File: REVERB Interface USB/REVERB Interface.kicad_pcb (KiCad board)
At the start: 2 copper layers, 90.2 x 95.9 mm, 60 parts, among them J1 RPiZeroW, J2 Iridium, J3 APRS, J4 Antenna, J6 USB_B_Micro, J7 USB, J8 USBPOGO, M1 MountingHole_Pad, M2 MountingHole_Pad, M3 MountingHole_Pad, M4 MountingHole_Pad, M5 PiMount, M6 PiMount, M7 PiMount, M8 PiMount, U1 LSM9DS1BOB, U2 MAX3232, U3 CY7C65213-28PVXI, U4 TXB0104D

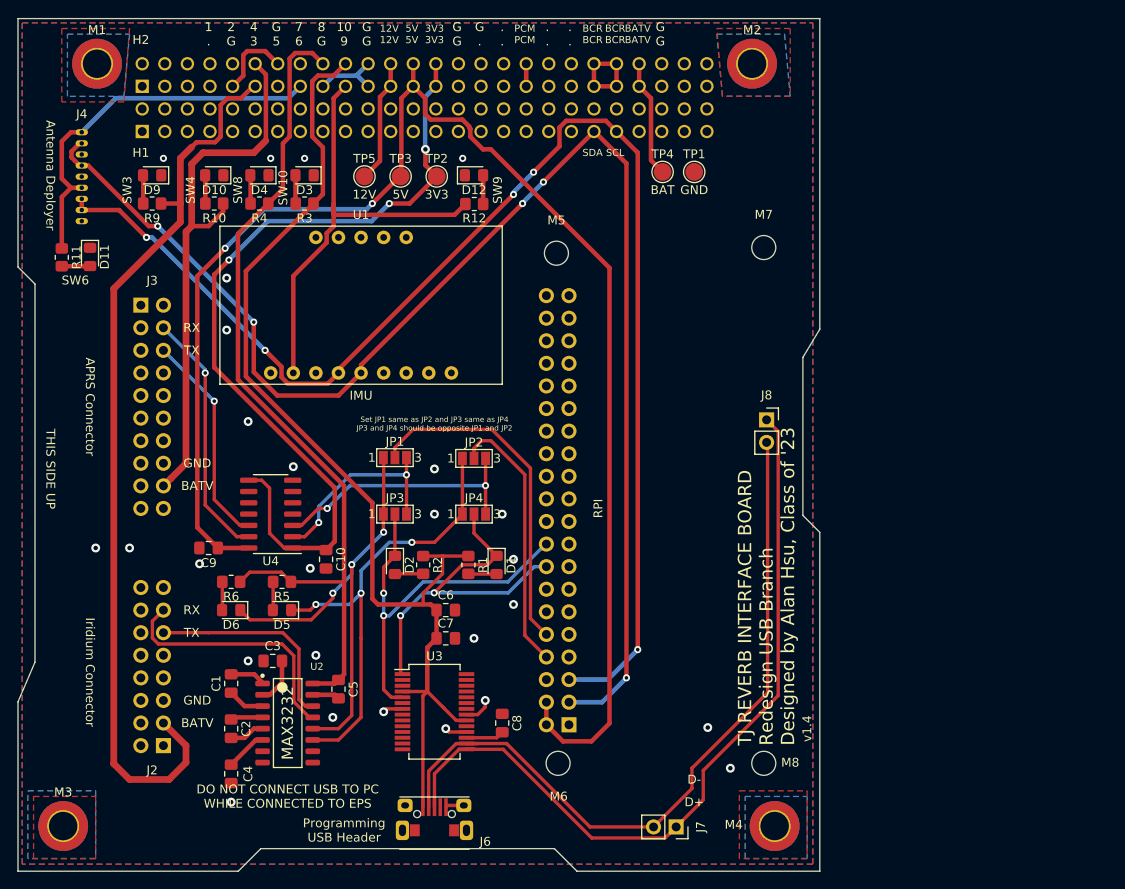
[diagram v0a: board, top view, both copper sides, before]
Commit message: Add decoupling
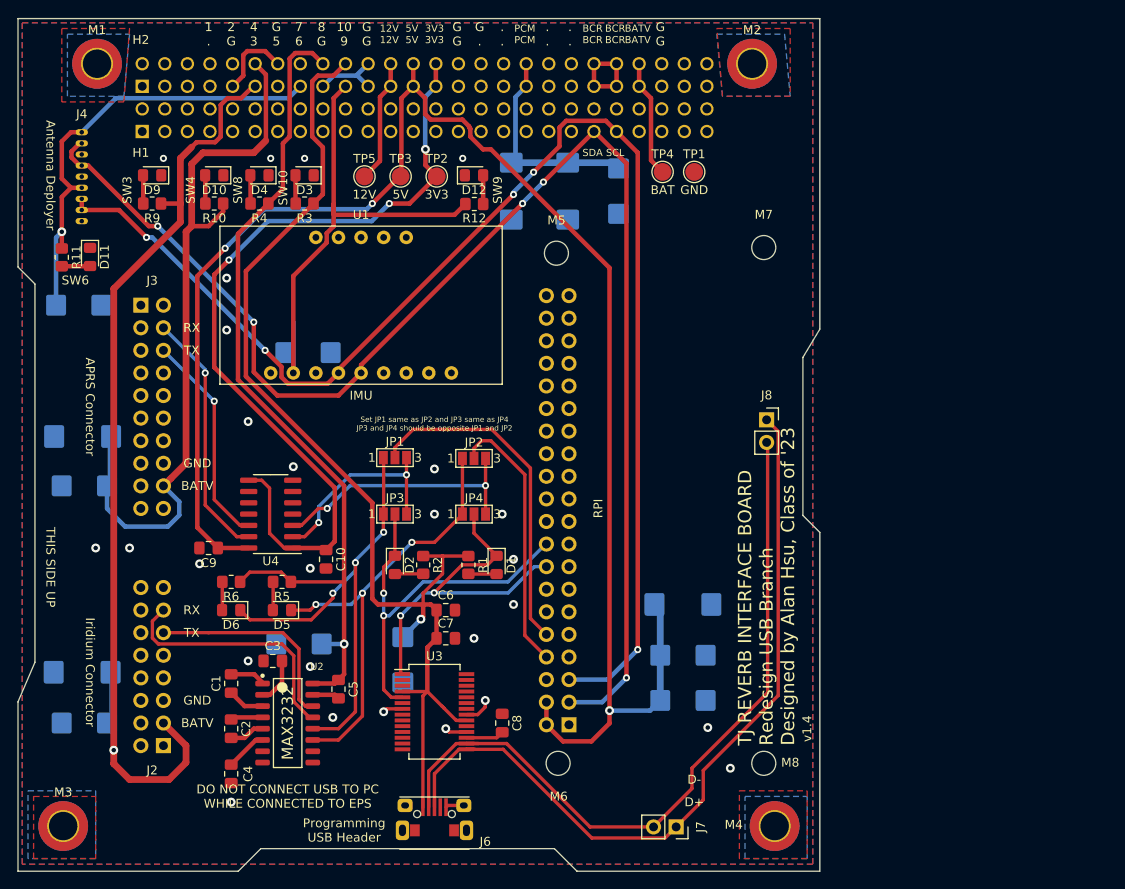
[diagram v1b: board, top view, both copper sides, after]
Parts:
- added C11: 100uF, Capacitor_Tantalum_SMD:CP_EIA-7343-43_Kemet-X_Pad2.25x2.55mm_HandSolder, B.Cu at (181.6, 118.7)
- added C12: 47uF, Capacitor_Tantalum_SMD:CP_EIA-6032-28_Kemet-C_Pad2.25x2.35mm_HandSolder, B.Cu at (181.6, 124.5)
- added C13: 22uF, Capacitor_Tantalum_SMD:CP_EIA-6032-28_Kemet-C_Pad2.25x2.35mm_HandSolder, B.Cu at (181.6, 129.5)
- added C14: 100uF, Capacitor_Tantalum_SMD:CP_EIA-7343-43_Kemet-X_Pad2.25x2.55mm_HandSolder, B.Cu at (114.0, 126.4)
- added C15: 47uF, Capacitor_Tantalum_SMD:CP_EIA-6032-28_Kemet-C_Pad2.25x2.35mm_HandSolder, B.Cu at (114.3, 132.1)
- added C16: 47uF, Capacitor_Tantalum_SMD:CP_EIA-6032-28_Kemet-C_Pad2.25x2.35mm_HandSolder, B.Cu at (113.7, 85.1)
- added C18: 47uF, Capacitor_Tantalum_SMD:CP_EIA-6032-28_Kemet-C_Pad2.25x2.35mm_HandSolder, B.Cu at (139.4, 90.4)
- added C20: 100uF, Capacitor_Tantalum_SMD:CP_EIA-7343-43_Kemet-X_Pad2.25x2.55mm_HandSolder, B.Cu at (162.3, 72.3)
- added C21: 100uF, Capacitor_Tantalum_SMD:CP_EIA-7343-43_Kemet-X_Pad2.25x2.55mm_HandSolder, B.Cu at (168.7, 72.3)
- added C22: 47uF, Capacitor_Tantalum_SMD:CP_EIA-6032-28_Kemet-C_Pad2.25x2.35mm_HandSolder, B.Cu at (174.4, 72.3)
- added C23: 100uF, Capacitor_Tantalum_SMD:CP_EIA-7343-43_Kemet-X_Pad2.25x2.55mm_HandSolder, B.Cu at (114.1, 99.9)
- added C24: 47uF, Capacitor_Tantalum_SMD:CP_EIA-6032-28_Kemet-C_Pad2.25x2.35mm_HandSolder, B.Cu at (114.3, 105.4)
- added C25: 47uF, Capacitor_Tantalum_SMD:CP_EIA-6032-28_Kemet-C_Pad2.25x2.35mm_HandSolder, B.Cu at (138.4, 123.2)
- added C27: 47uF, Capacitor_Tantalum_SMD:CP_EIA-6032-28_Kemet-C_Pad2.25x2.35mm_HandSolder, B.Cu at (150.1, 125.0)
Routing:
- net /SW4: track 61.2 -> 83.0 mm
- net /PCM_IN: track 2.54 -> 24.2 mm
- net +5V: track 170.4 -> 187.6 mm, vias 2 -> 3
- net /SW3: track 104.9 -> 114.2 mm, vias 0 -> 1
- net /SW6: track 43.5 -> 51.7 mm, vias 0 -> 1
- net /SW9: track 51.1 -> 56.8 mm
- net /SW10: track 125.2 -> 129.8 mm, vias 0 -> 1
- net /SW8: track 97.7 -> 100.3 mm, vias 0 -> 1
- net /T1IN: track 52.0 -> 50.7 mm

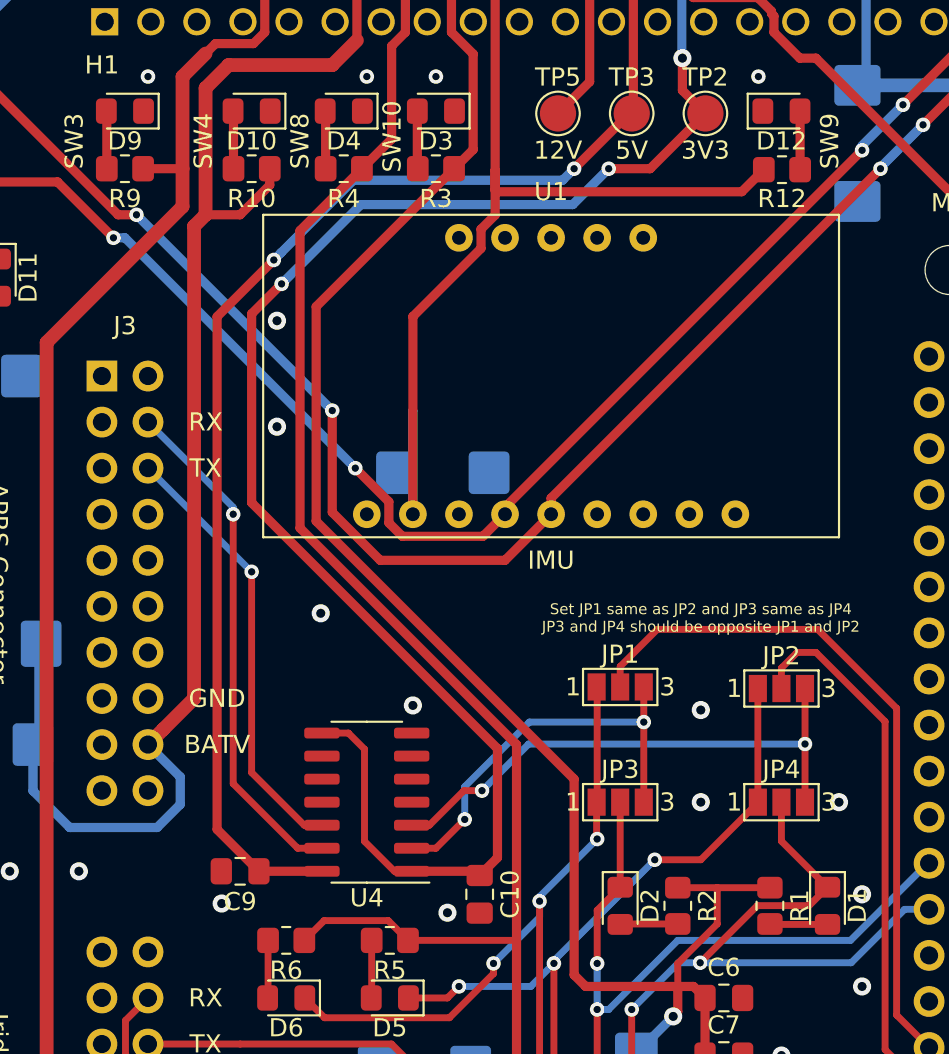
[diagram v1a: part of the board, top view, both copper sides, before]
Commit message: fix imu implementation, add bno055 compatibility
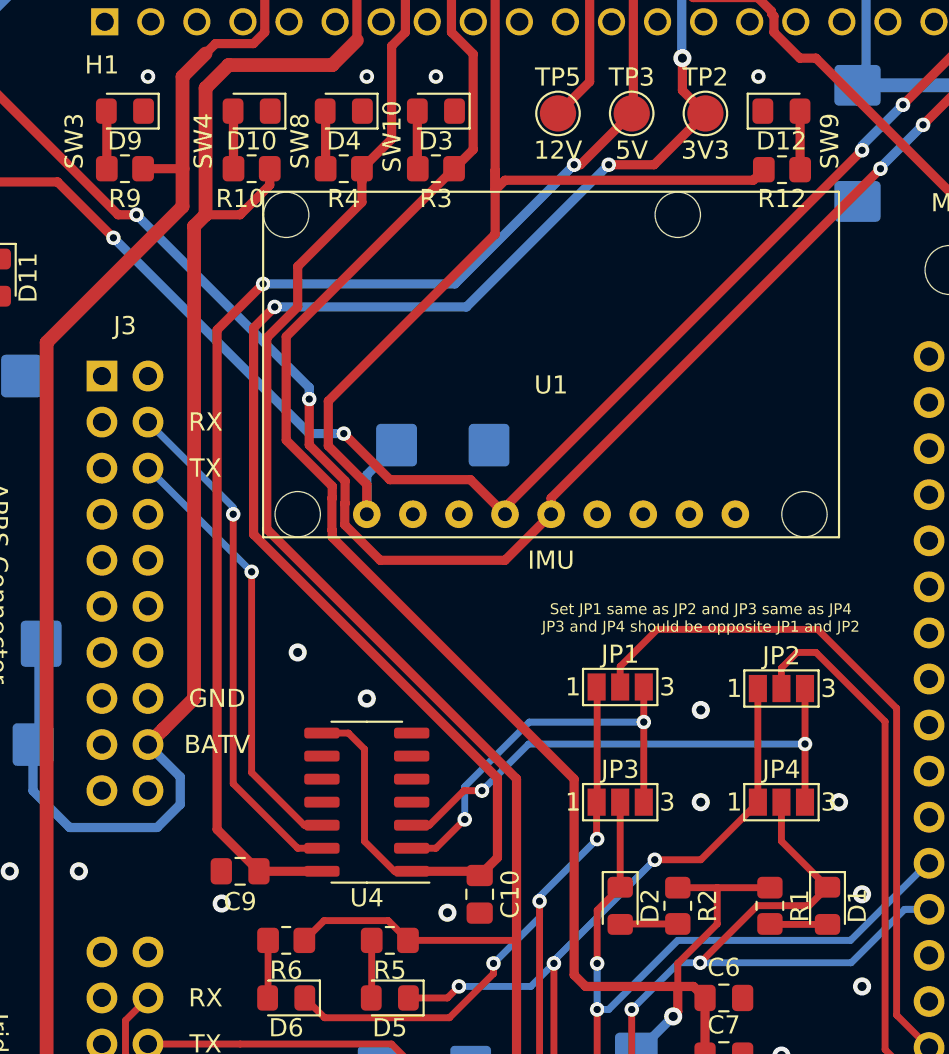
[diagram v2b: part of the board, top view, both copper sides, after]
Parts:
- U1: value LSM9DS1BOB -> IMU; footprint REVERB Interface:LSM9DS1BOB -> REVERB Interface:LSM9DS1-BNO055
- moved C18 1.52 mm to (139.4, 88.9)
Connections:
- U1 pad 1: (no net) -> /SW9
- U1 pad 3: (no net) -> GND
- U1 pad 4: (no net) -> /EPSSCL
- U1 pad 5: (no net) -> /EPSSDA
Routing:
- net /EPSSCL: track 152.9 -> 151.2 mm
- net /SW8: track 100.3 -> 101.8 mm
- net /SW9: track 56.8 -> 58.3 mm
- net /SW10: track 129.8 -> 131.2 mm
- net +3V3: track 95.2 -> 94.6 mm
- net GND: vias 27 -> 25

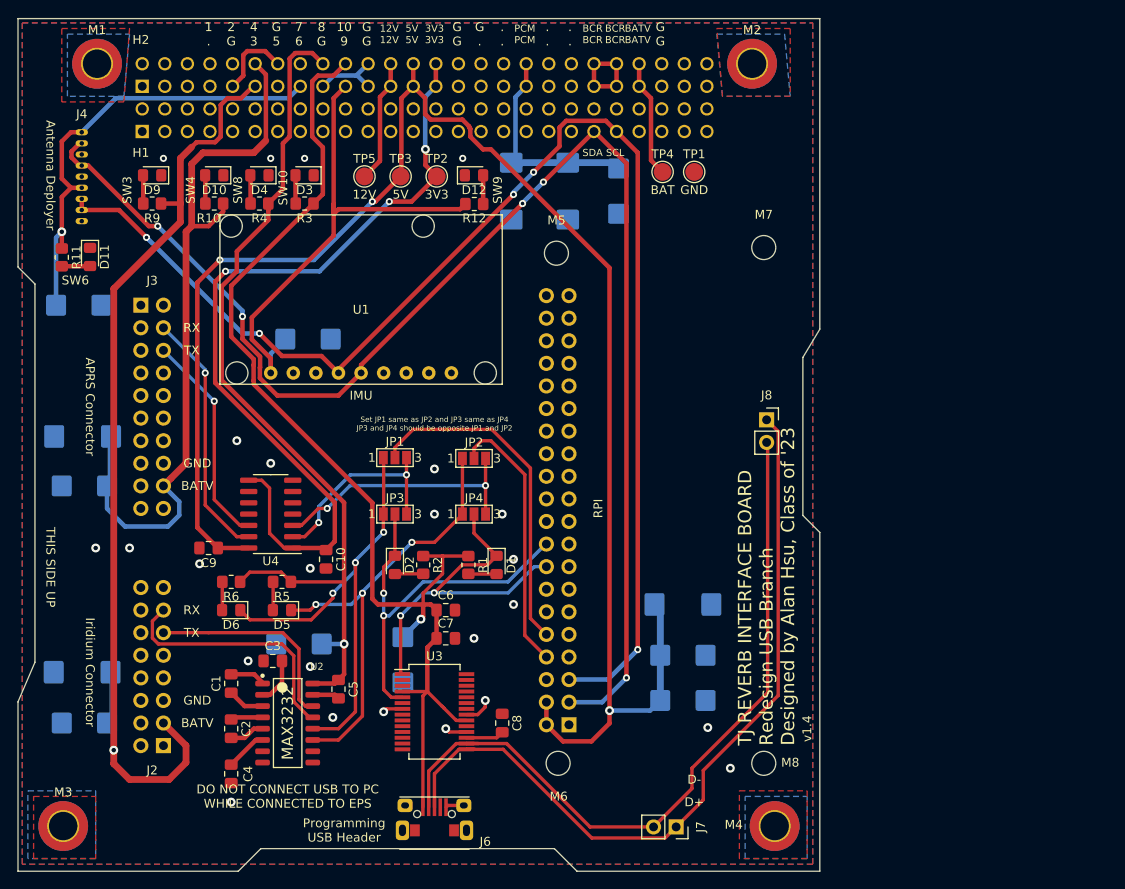
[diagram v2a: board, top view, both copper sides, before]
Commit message: finish bno055 mod, push v1.5
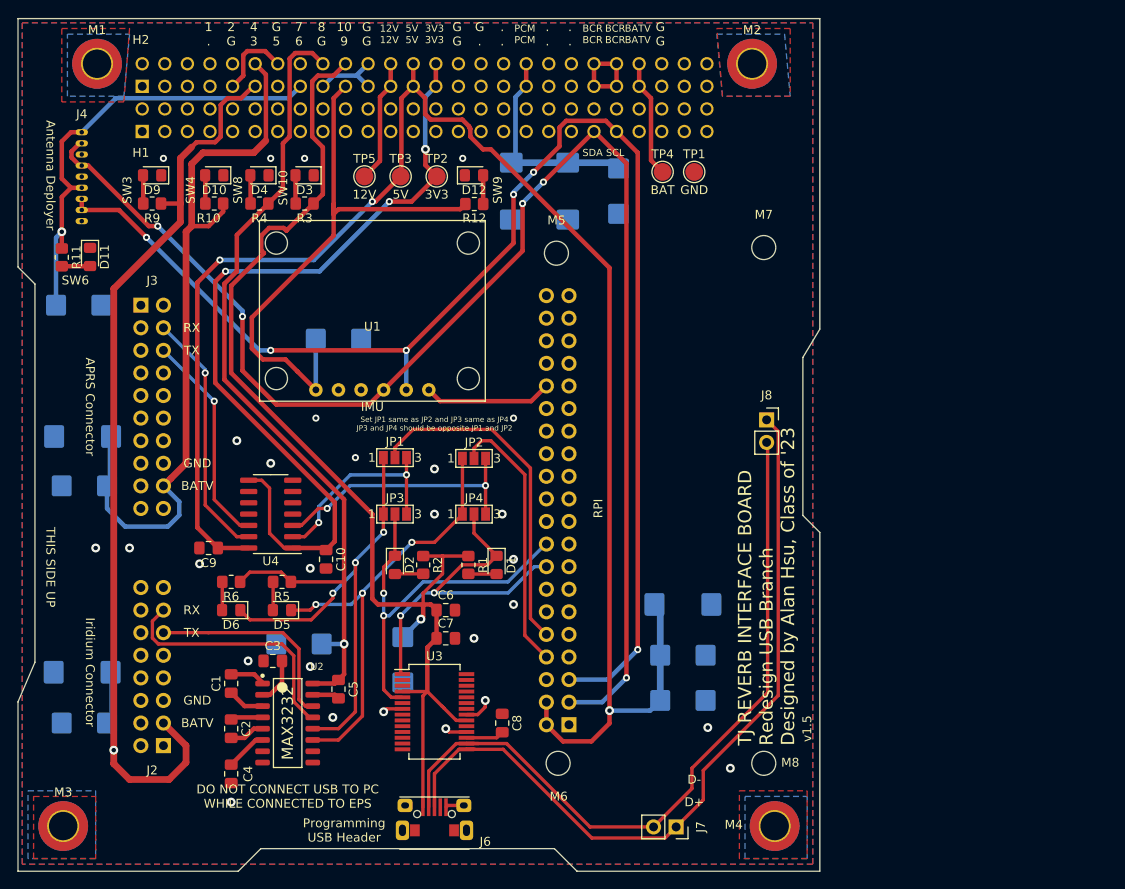
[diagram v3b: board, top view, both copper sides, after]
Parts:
- U1: footprint REVERB Interface:LSM9DS1-BNO055 -> REVERB Interface:BNO055
- moved C18 3.43 mm to (142.9, 88.9)
- moved U1 1.42 mm to (146.7, 85.7)
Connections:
- J1 pad 32: (no net) -> /IMURST
- U1 pad 4: /EPSSCL -> /EPSSDA
- U1 pad 5: /EPSSDA -> /EPSSCL
- U1 pad 6: (no net) -> /IMURST
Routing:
- net /IMURST: track 0.00 -> 14.5 mm
- net /SW9: track 58.3 -> 65.1 mm
- net /EPSSCL: track 151.2 -> 156.5 mm, vias 5 -> 6
- net /EPSSDA: track 158.8 -> 162.9 mm
- net /SW10: track 131.2 -> 133.0 mm
- net GND: vias 25 -> 28
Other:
- board text added: "v1.5"
- board text removed: "v1.4"

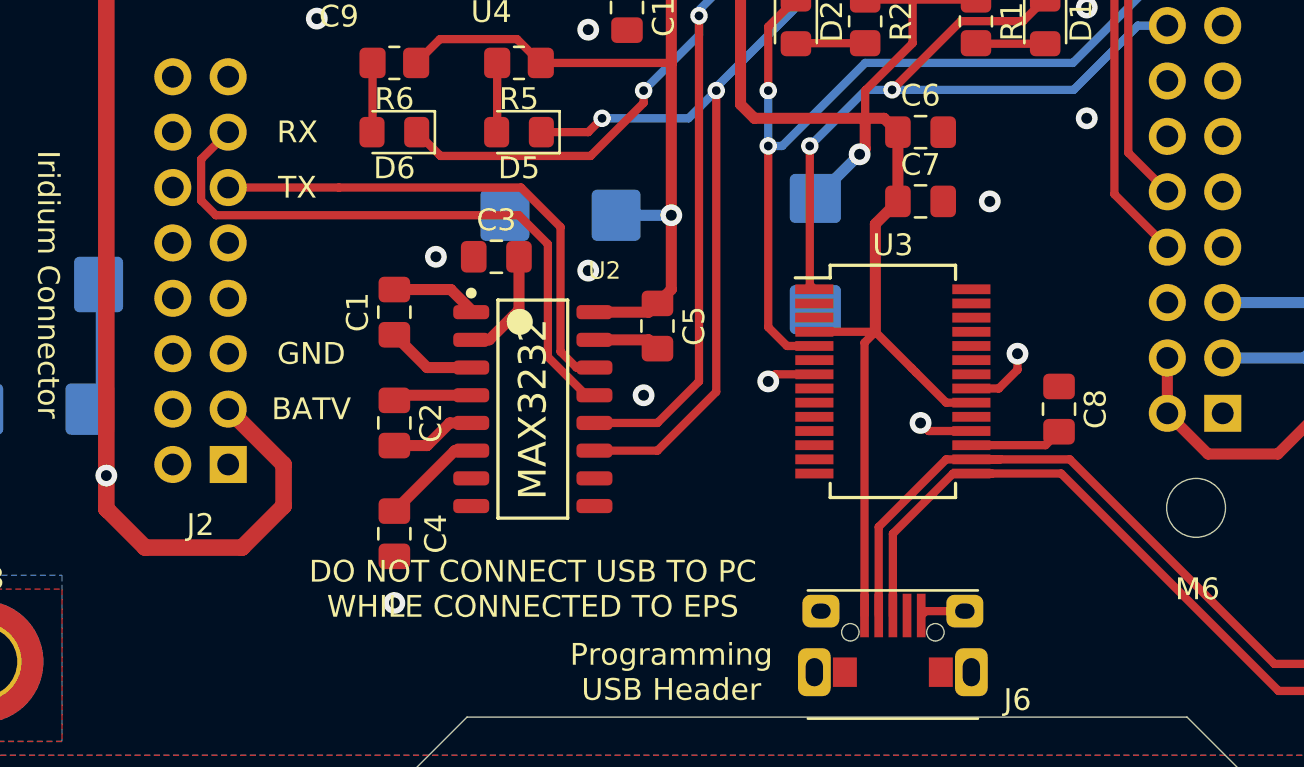
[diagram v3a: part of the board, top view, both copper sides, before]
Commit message: route, edit i2c description
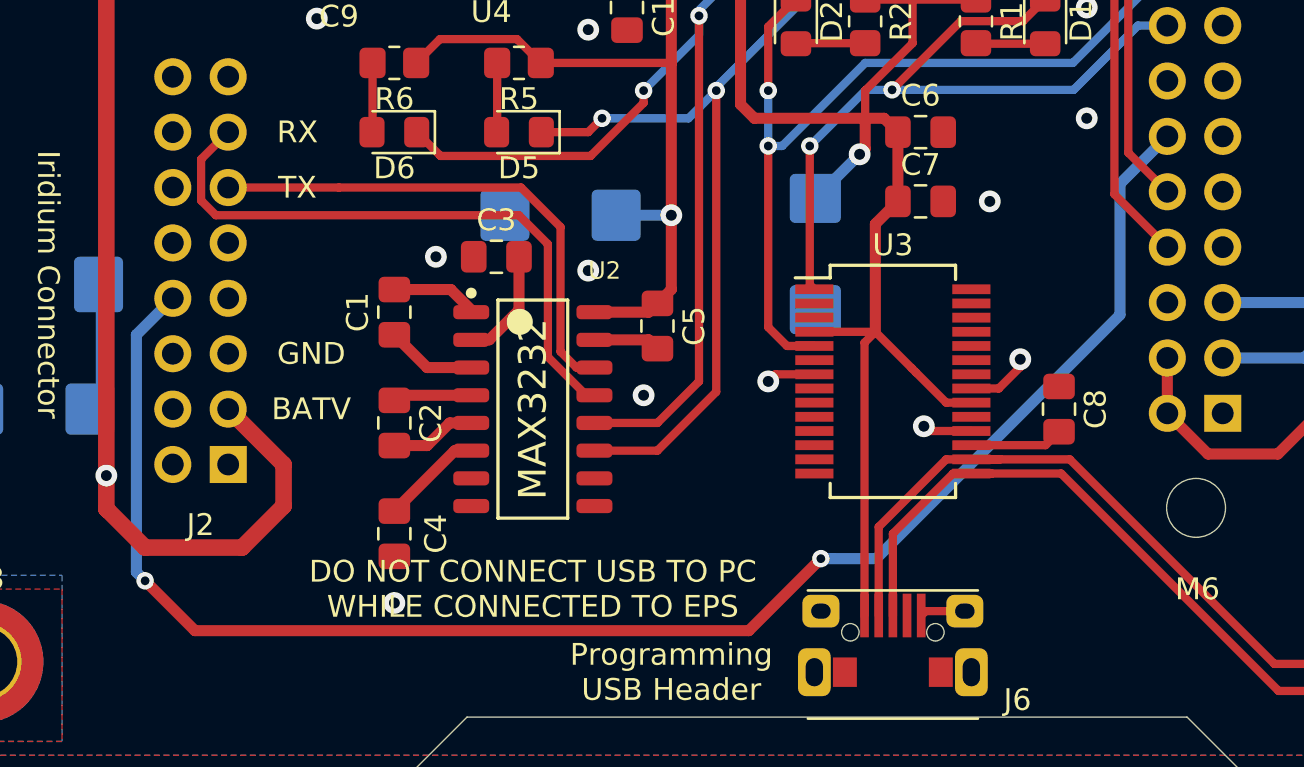
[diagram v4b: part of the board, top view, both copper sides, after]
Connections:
- J1 pad 12: (no net) -> /RI
- J2 pad 15: (no net) -> GND
- J2 pad 8: (no net) -> /RI
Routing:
- net /RI: track 0.00 -> 74.5 mm, vias 0 -> 2
